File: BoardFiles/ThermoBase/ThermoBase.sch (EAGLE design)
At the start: 22 parts, among them CON1 BARREL_JACK_3PIN, U1 MOSFET_N, U2 MOSFET_N, U3 MOSFET_N, U4 LM317

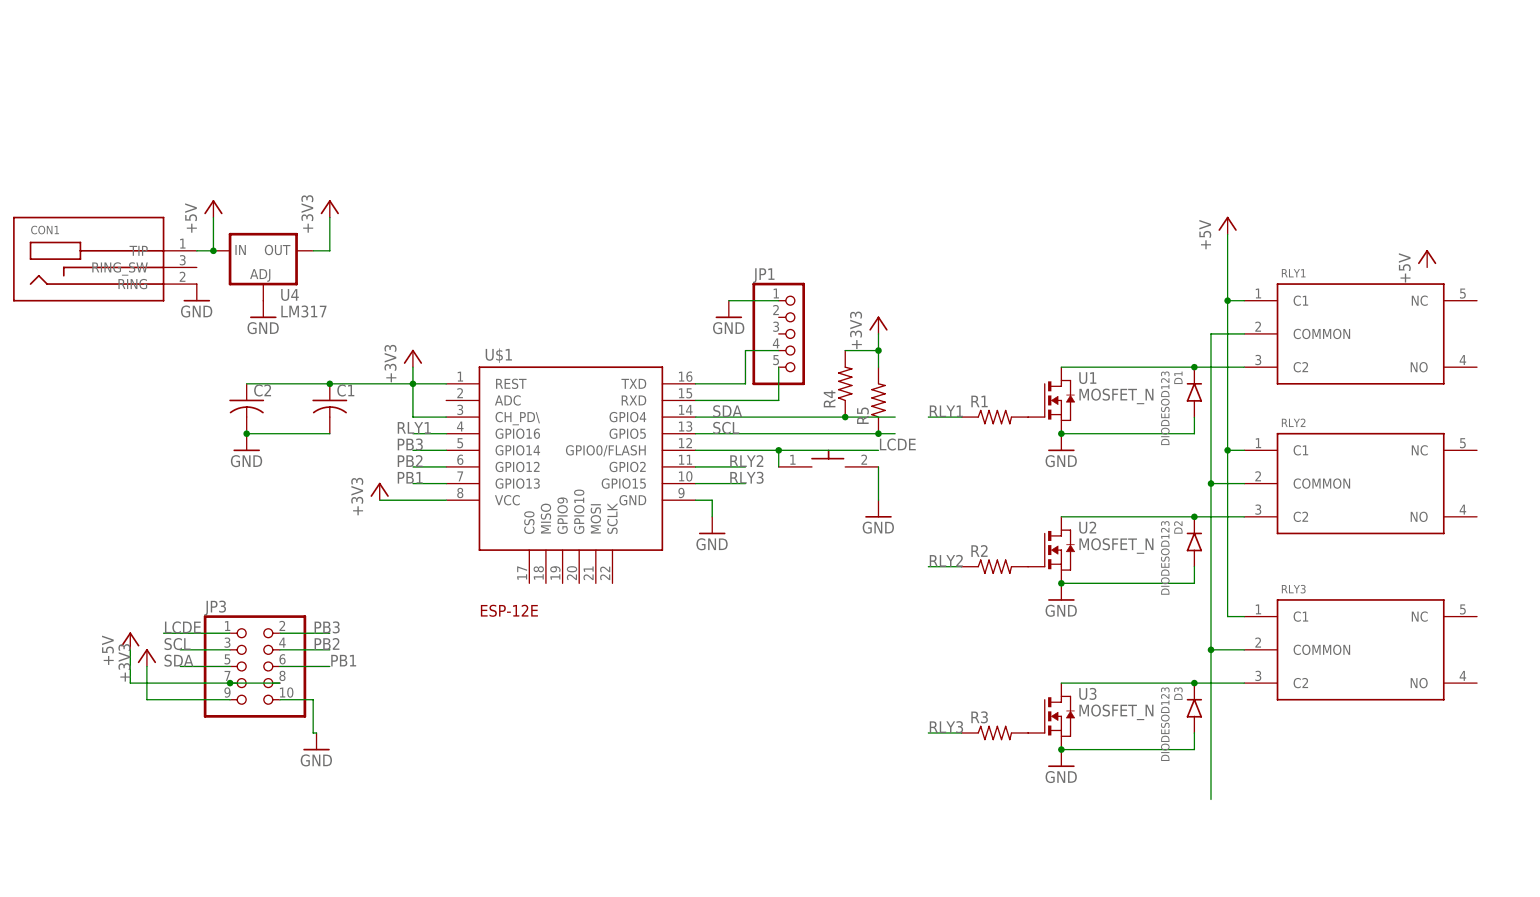
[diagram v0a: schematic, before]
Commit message: Created LCD Screen holder and updated base board to fit enclosure
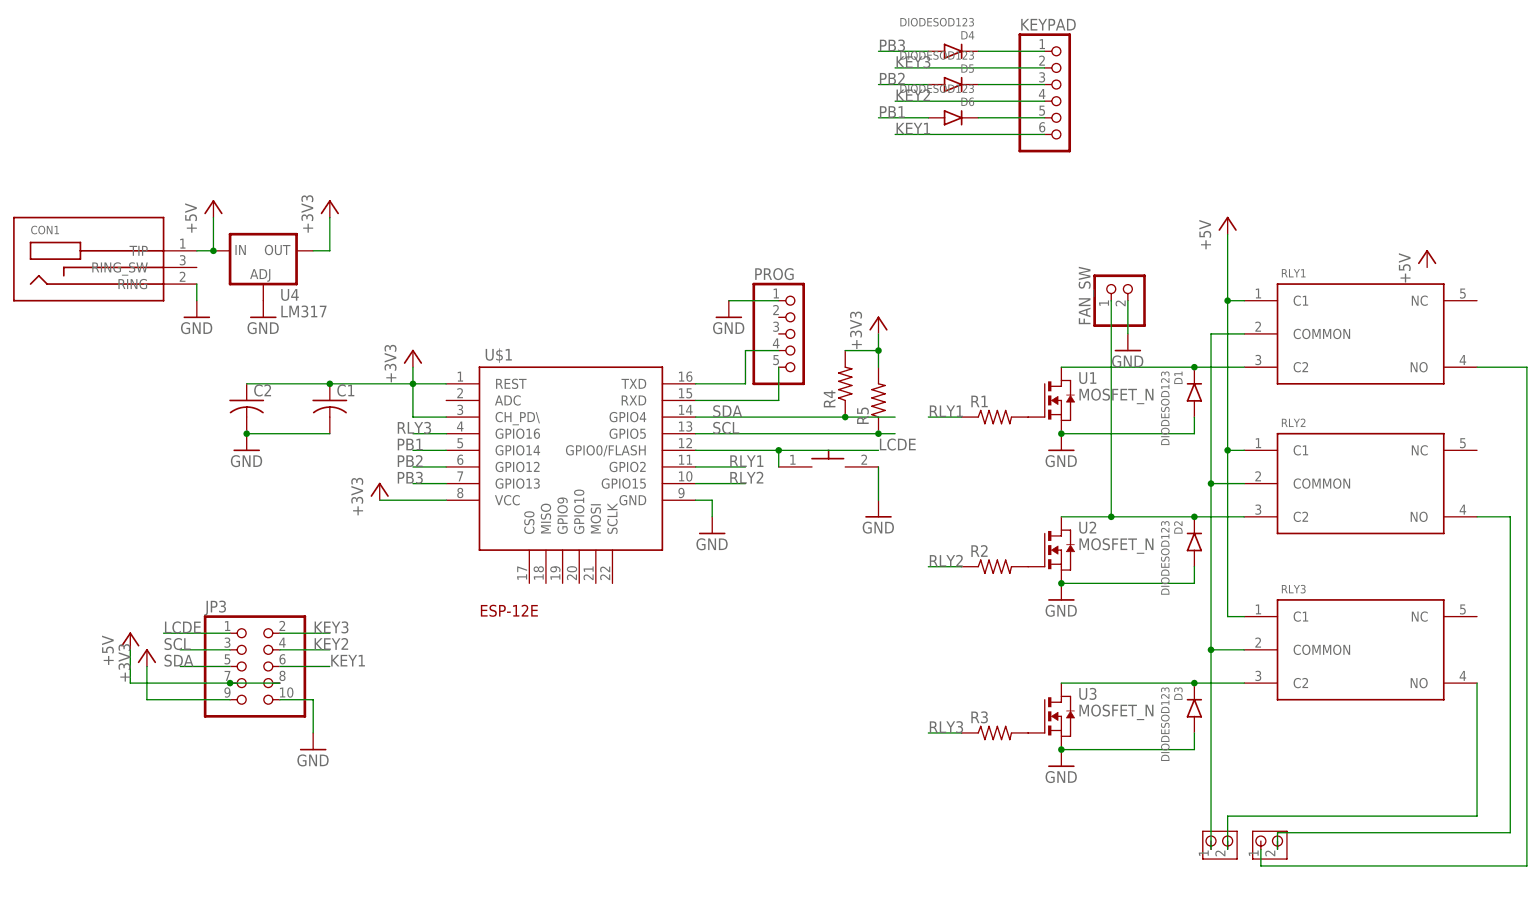
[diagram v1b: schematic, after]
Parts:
- added D4, D5, D6: DIODESOD123, DR:DIODESOD123
- added FAN_SW: (no value), pinhead:PINHD-1X2
- added H1, H2: TERMBLOCK_5MM_2POS, DR:TERMBLOCK_5MM_2POS
- added KEYPAD: (no value), pinhead:PINHD-1X6
- renumbered JP1 to PROG
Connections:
- new net KEY1: JP3.6, KEYPAD.6
- new net KEY2: JP3.4, KEYPAD.4
- new net KEY3: JP3.2, KEYPAD.2
- new net N$12: H1.2, RLY3.NO
- new net N$13: D4.C, KEYPAD.1
- new net N$14: D5.C, KEYPAD.3
- new net N$15: D6.C, KEYPAD.5
- new net N$3: H2.1, RLY1.NO
- new net N$8: H2.2, RLY2.NO
- net GND: now also FAN_SW.2
- net N$11: now also H1.1
- net N$9: now also FAN_SW.1
- net PB1: now also D6.A, U$1.GPIO14; no longer JP3.6, U$1.GPIO13
- net PB2: now also D5.A; no longer JP3.4
- net PB3: now also D4.A, U$1.GPIO13; no longer JP3.2, U$1.GPIO14
- net RLY1: now also U$1.GPIO2; no longer U$1.GPIO16
- net RLY2: now also U$1.GPIO15; no longer U$1.GPIO2
- net RLY3: now also U$1.GPIO16; no longer U$1.GPIO15

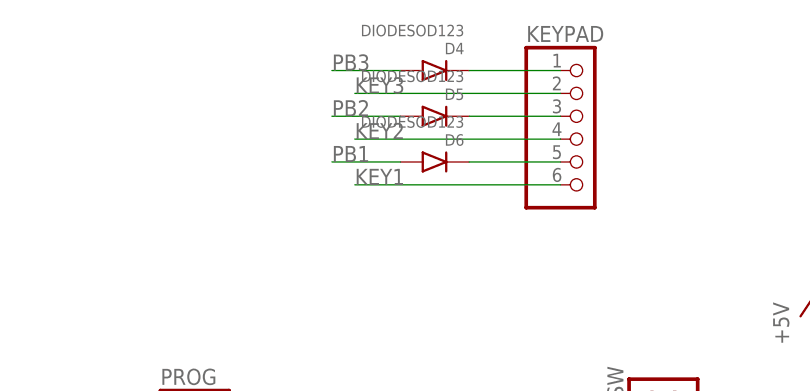
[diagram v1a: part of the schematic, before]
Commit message: Successfully built display board, archived old test software
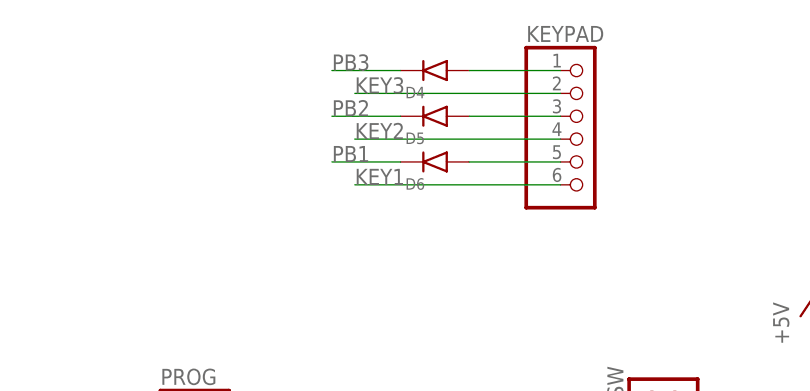
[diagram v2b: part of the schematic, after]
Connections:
- net N$13: now also D4.A; no longer D4.C
- net N$14: now also D5.A; no longer D5.C
- net N$15: now also D6.A; no longer D6.C
- net PB1: now also D6.C; no longer D6.A
- net PB2: now also D5.C; no longer D5.A
- net PB3: now also D4.C; no longer D4.A
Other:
- moved on the sheet: D4, D5, D6
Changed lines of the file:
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@@
 <part name="FAN_SW" library="pinhead" library_urn="urn:adsk.eagle:library:325" deviceset="PINHD-1X2" device="" package3d_urn="urn:adsk.eagle:package:22435/2"/>
 <part name="GND11" library="supply1" library_urn="urn:adsk.eagle:library:371" deviceset="GND" device=""/>
+<part name="KEYPAD" library="pinhead" library_urn="urn:adsk.eagle:library:325" deviceset="PINHD-1X6" device="" package3d_urn="urn:adsk.eagle:package:22472/2"/>
 <part name="D4" library="DR" deviceset="DIODE" device="SOD123"/>
-<part name="KEYPAD" library="pinhead" library_urn="urn:adsk.eagle:library:325" deviceset="PINHD-1X6" device="" package3d_urn="urn:adsk.eagle:package:22472/2"/>
 <part name="D5" library="DR" deviceset="DIODE" device="SOD123"/>
 <part name="D6" library="DR" deviceset="DIODE" device="SOD123"/>
@@
 <attribute name="VALUE" x="152.4" y="55.88" size="1.778" layer="96"/>
 </instance>
-<instance part="D4" gate="G$1" x="127" y="104.14" smashed="yes" rot="R90">
-<attribute name="NAME" x="131.556" y="107.22" size="1.27" layer="95" rot="R180"/>
-<attribute name="VALUE" x="131.556" y="109.22" size="1.27" layer="96" rot="R180"/>
-</instance>
 <instance part="KEYPAD" gate="A" x="144.78" y="96.52" smashed="yes">
 <attribute name="NAME" x="138.43" y="107.315" size="1.778" layer="95"/>
 <attribute name="VALUE" x="138.43" y="86.36" size="1.778" layer="96"/>
 </instance>
-<instance part="D5" gate="G$1" x="127" y="99.06" smashed="yes" rot="R90">
-<attribute name="NAME" x="131.556" y="102.14" size="1.27" layer="95" rot="R180"/>
-<attribute name="VALUE" x="131.556" y="104.14" size="1.27" layer="96" rot="R180"/>
-</instance>
-<instance part="D6" gate="G$1" x="127" y="93.98" smashed="yes" rot="R90">
-<attribute name="NAME" x="131.556" y="97.06" size="1.27" layer="95" rot="R180"/>
-<attribute name="VALUE" x="131.556" y="99.06" size="1.27" layer="96" rot="R180"/>
+<instance part="D4" gate="G$1" x="129.54" y="104.14" smashed="yes" rot="R270">
+<attribute name="NAME" x="124.984" y="101.06" size="1.27" layer="95"/>
+</instance>
+<instance part="D5" gate="G$1" x="129.54" y="99.06" smashed="yes" rot="R270">
+<attribute name="NAME" x="124.984" y="95.98" size="1.27" layer="95"/>
+</instance>
+<instance part="D6" gate="G$1" x="129.54" y="93.98" smashed="yes" rot="R270">
+<attribute name="NAME" x="124.984" y="90.9" size="1.27" layer="95"/>
 </instance>
 </instances>
@@
 <segment>
 <wire x1="124.46" y1="93.98" x2="116.84" y2="93.98" width="0.1524" layer="91"/>
-<pinref part="D6" gate="G$1" pin="A"/>
 <label x="116.84" y="93.98" size="1.778" layer="95"/>
+<pinref part="D6" gate="G$1" pin="C"/>
 </segment>
 <segment>
@@
 <segment>
 <wire x1="124.46" y1="99.06" x2="116.84" y2="99.06" width="0.1524" layer="91"/>
-<pinref part="D5" gate="G$1" pin="A"/>
 <label x="116.84" y="99.06" size="1.778" layer="95"/>
+<pinref part="D5" gate="G$1" pin="C"/>
 </segment>
 </net>
@@
 <segment>
 <wire x1="124.46" y1="104.14" x2="116.84" y2="104.14" width="0.1524" layer="91"/>
-<pinref part="D4" gate="G$1" pin="A"/>
 <label x="116.84" y="104.14" size="1.778" layer="95"/>
+<pinref part="D4" gate="G$1" pin="C"/>
 </segment>
 <segment>
@@
 <segment>
 <pinref part="KEYPAD" gate="A" pin="1"/>
-<pinref part="D4" gate="G$1" pin="C"/>
 <wire x1="142.24" y1="104.14" x2="132.08" y2="104.14" width="0.1524" layer="91"/>
+<pinref part="D4" gate="G$1" pin="A"/>
 </segment>
 </net>
@@
 <segment>
 <pinref part="KEYPAD" gate="A" pin="3"/>
-<pinref part="D5" gate="G$1" pin="C"/>
 <wire x1="142.24" y1="99.06" x2="132.08" y2="99.06" width="0.1524" layer="91"/>
+<pinref part="D5" gate="G$1" pin="A"/>
 </segment>
 </net>
@@
 <segment>
 <pinref part="KEYPAD" gate="A" pin="5"/>
-<pinref part="D6" gate="G$1" pin="C"/>
 <wire x1="142.24" y1="93.98" x2="132.08" y2="93.98" width="0.1524" layer="91"/>
-</segment>
-</net>
+<pinref part="D6" gate="G$1" pin="A"/>
+</segment>
+</net>

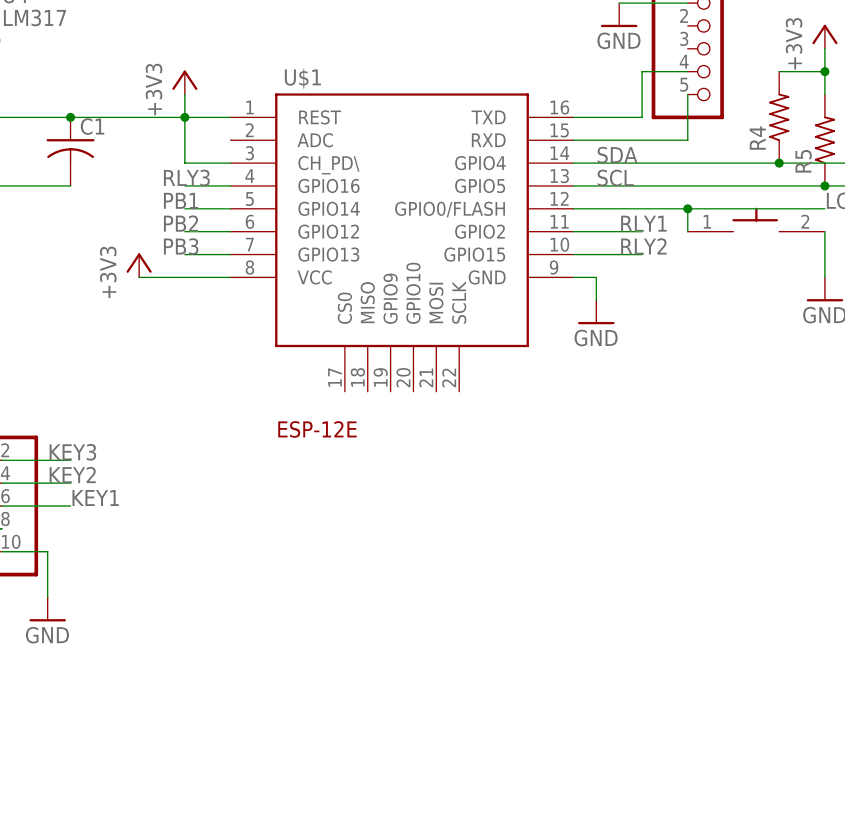
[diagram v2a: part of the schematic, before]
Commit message: Changes for keypad
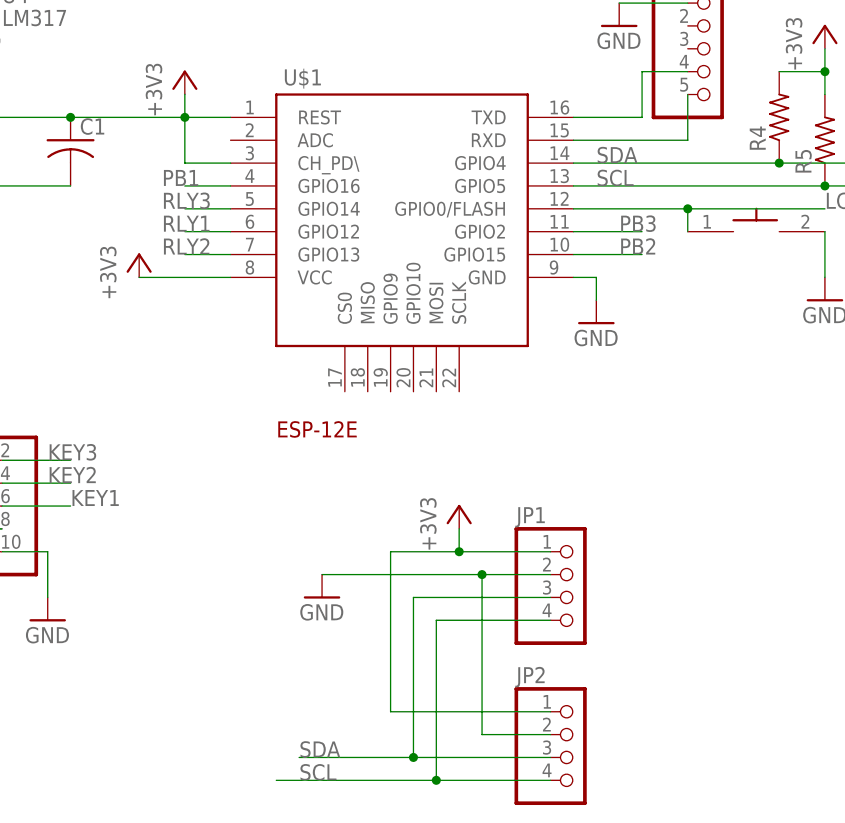
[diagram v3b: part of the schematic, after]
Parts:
- added JP1, JP2: (no value), pinhead:PINHD-1X4
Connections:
- net +3V3: now also JP1.1, JP2.1
- net GND: now also JP1.2, JP2.2
- net PB1: now also U$1.GPIO16; no longer U$1.GPIO14
- net PB2: now also U$1.GPIO15; no longer U$1.GPIO12
- net PB3: now also U$1.GPIO2; no longer U$1.GPIO13
- net RLY1: now also U$1.GPIO12; no longer U$1.GPIO2
- net RLY2: now also U$1.GPIO13; no longer U$1.GPIO15
- net RLY3: now also U$1.GPIO14; no longer U$1.GPIO16
- net SCL: now also JP1.4, JP2.4
- net SDA: now also JP1.3, JP2.3
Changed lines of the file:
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@@
 <part name="D5" library="DR" deviceset="DIODE" device="SOD123"/>
 <part name="D6" library="DR" deviceset="DIODE" device="SOD123"/>
+<part name="JP1" library="pinhead" library_urn="urn:adsk.eagle:library:325" deviceset="PINHD-1X4" device="" package3d_urn="urn:adsk.eagle:package:22407/2"/>
+<part name="JP2" library="pinhead" library_urn="urn:adsk.eagle:library:325" deviceset="PINHD-1X4" device="" package3d_urn="urn:adsk.eagle:package:22407/2"/>
+<part name="+3V6" library="supply1" library_urn="urn:adsk.eagle:library:371" deviceset="+3V3" device=""/>
+<part name="GND12" library="supply1" library_urn="urn:adsk.eagle:library:371" deviceset="GND" device=""/>
 </parts>
 <sheets>
@@
 <attribute name="NAME" x="124.984" y="90.9" size="1.27" layer="95"/>
 </instance>
+<instance part="JP1" gate="A" x="88.9" y="0" smashed="yes">
+<attribute name="NAME" x="82.55" y="8.255" size="1.778" layer="95"/>
+<attribute name="VALUE" x="82.55" y="-7.62" size="1.778" layer="96"/>
+</instance>
+<instance part="JP2" gate="A" x="88.9" y="-17.78" smashed="yes">
+<attribute name="NAME" x="82.55" y="-9.525" size="1.778" layer="95"/>
+<attribute name="VALUE" x="82.55" y="-25.4" size="1.778" layer="96"/>
+</instance>
+<instance part="+3V6" gate="G$1" x="76.2" y="10.16" smashed="yes">
+<attribute name="VALUE" x="73.66" y="5.08" size="1.778" layer="96" rot="R90"/>
+</instance>
+<instance part="GND12" gate="1" x="60.96" y="0" smashed="yes">
+<attribute name="VALUE" x="58.42" y="-2.54" size="1.778" layer="96"/>
+</instance>
 </instances>
 <busses>
@@
 <pinref part="FAN_SW" gate="G$1" pin="2"/>
 <wire x1="154.94" y1="60.96" x2="154.94" y2="66.04" width="0.1524" layer="91"/>
+</segment>
+<segment>
+<pinref part="GND12" gate="1" pin="GND"/>
+<pinref part="JP1" gate="A" pin="2"/>
+<wire x1="60.96" y1="2.54" x2="78.74" y2="2.54" width="0.1524" layer="91"/>
+<pinref part="JP2" gate="A" pin="2"/>
+<wire x1="78.74" y1="2.54" x2="86.36" y2="2.54" width="0.1524" layer="91"/>
+<wire x1="86.36" y1="-15.24" x2="78.74" y2="-15.24" width="0.1524" layer="91"/>
+<wire x1="78.74" y1="-15.24" x2="78.74" y2="2.54" width="0.1524" layer="91"/>
+<junction x="78.74" y="2.54"/>
 </segment>
 </net>
@@
 <junction x="116.84" y="58.42"/>
 </segment>
+<segment>
+<pinref part="JP1" gate="A" pin="1"/>
+<pinref part="+3V6" gate="G$1" pin="+3V3"/>
+<wire x1="86.36" y1="5.08" x2="76.2" y2="5.08" width="0.1524" layer="91"/>
+<wire x1="76.2" y1="5.08" x2="76.2" y2="7.62" width="0.1524" layer="91"/>
+<wire x1="76.2" y1="5.08" x2="68.58" y2="5.08" width="0.1524" layer="91"/>
+<junction x="76.2" y="5.08"/>
+<wire x1="68.58" y1="5.08" x2="68.58" y2="-12.7" width="0.1524" layer="91"/>
+<pinref part="JP2" gate="A" pin="1"/>
+<wire x1="68.58" y1="-12.7" x2="86.36" y2="-12.7" width="0.1524" layer="91"/>
+</segment>
 </net>
 <net name="SDA" class="0">
@@
 <label x="7.62" y="10.16" size="1.778" layer="95"/>
 </segment>
+<segment>
+<wire x1="58.42" y1="-17.78" x2="71.12" y2="-17.78" width="0.1524" layer="91"/>
+<pinref part="JP1" gate="A" pin="3"/>
+<wire x1="71.12" y1="-17.78" x2="86.36" y2="-17.78" width="0.1524" layer="91"/>
+<wire x1="86.36" y1="0" x2="71.12" y2="0" width="0.1524" layer="91"/>
+<wire x1="71.12" y1="0" x2="71.12" y2="-17.78" width="0.1524" layer="91"/>
+<junction x="71.12" y="-17.78"/>
+<pinref part="JP2" gate="A" pin="3"/>
+<label x="58.42" y="-17.78" size="1.778" layer="95"/>
+</segment>
 </net>
 <net name="SCL" class="0">
@@
 <label x="7.62" y="12.7" size="1.778" layer="95"/>
 </segment>
+<segment>
+<wire x1="55.88" y1="-20.32" x2="73.66" y2="-20.32" width="0.1524" layer="91"/>
+<pinref part="JP1" gate="A" pin="4"/>
+<wire x1="73.66" y1="-20.32" x2="86.36" y2="-20.32" width="0.1524" layer="91"/>
+<wire x1="86.36" y1="-2.54" x2="73.66" y2="-2.54" width="0.1524" layer="91"/>
+<wire x1="73.66" y1="-2.54" x2="73.66" y2="-20.32" width="0.1524" layer="91"/>
+<junction x="73.66" y="-20.32"/>
+<pinref part="JP2" gate="A" pin="4"/>
+<label x="58.42" y="-20.32" size="1.778" layer="95"/>
+</segment>
 </net>
 <net name="RLY1" class="0">
@@
 </segment>
 <segment>
-<pinref part="U$1" gate="G$1" pin="GPIO2"/>
-<wire x1="88.9" y1="40.64" x2="96.52" y2="40.64" width="0.1524" layer="91"/>
-<label x="93.98" y="40.64" size="1.778" layer="95"/>
+<pinref part="U$1" gate="G$1" pin="GPIO12"/>
+<wire x1="50.8" y1="40.64" x2="45.72" y2="40.64" width="0.1524" layer="91"/>
+<label x="43.18" y="40.64" size="1.778" layer="95"/>
 </segment>
 </net>
@@
 </segment>
 <segment>
-<pinref part="U$1" gate="G$1" pin="GPIO15"/>
-<wire x1="88.9" y1="38.1" x2="96.52" y2="38.1" width="0.1524" layer="91"/>
-<label x="93.98" y="38.1" size="1.778" layer="95"/>
+<pinref part="U$1" gate="G$1" pin="GPIO13"/>
+<wire x1="50.8" y1="38.1" x2="45.72" y2="38.1" width="0.1524" layer="91"/>
+<label x="43.18" y="38.1" size="1.778" layer="95"/>
 </segment>
 </net>
@@
 </segment>
 <segment>
-<pinref part="U$1" gate="G$1" pin="GPIO16"/>
-<wire x1="50.8" y1="45.72" x2="45.72" y2="45.72" width="0.1524" layer="91"/>
-<label x="43.18" y="45.72" size="1.778" layer="95"/>
+<pinref part="U$1" gate="G$1" pin="GPIO14"/>
+<wire x1="50.8" y1="43.18" x2="45.72" y2="43.18" width="0.1524" layer="91"/>
+<label x="43.18" y="43.18" size="1.778" layer="95"/>
 </segment>
 </net>
@@
 </segment>
 <segment>
-<pinref part="U$1" gate="G$1" pin="GPIO14"/>
-<wire x1="50.8" y1="43.18" x2="45.72" y2="43.18" width="0.1524" layer="91"/>
-<label x="43.18" y="43.18" size="1.778" layer="95"/>
+<pinref part="U$1" gate="G$1" pin="GPIO16"/>
+<wire x1="50.8" y1="45.72" x2="45.72" y2="45.72" width="0.1524" layer="91"/>
+<label x="43.18" y="45.72" size="1.778" layer="95"/>
 </segment>
 </net>
 <net name="PB2" class="0">
-<segment>
-<pinref part="U$1" gate="G$1" pin="GPIO12"/>
-<wire x1="50.8" y1="40.64" x2="45.72" y2="40.64" width="0.1524" layer="91"/>
-<label x="43.18" y="40.64" size="1.778" layer="95"/>
-</segment>
 <segment>
 <wire x1="124.46" y1="99.06" x2="116.84" y2="99.06" width="0.1524" layer="91"/>
@@
 <pinref part="D5" gate="G$1" pin="C"/>
 </segment>
+<segment>
+<pinref part="U$1" gate="G$1" pin="GPIO15"/>
+<wire x1="88.9" y1="38.1" x2="96.52" y2="38.1" width="0.1524" layer="91"/>
+<label x="93.98" y="38.1" size="1.778" layer="95"/>
+</segment>
 </net>
 <net name="PB3" class="0">
@@
 </segment>
 <segment>
-<pinref part="U$1" gate="G$1" pin="GPIO13"/>
-<wire x1="50.8" y1="38.1" x2="45.72" y2="38.1" width="0.1524" layer="91"/>
-<label x="43.18" y="38.1" size="1.778" layer="95"/>
-</segment>
-</net>
+<pinref part="U$1" gate="G$1" pin="GPIO2"/>
+<wire x1="88.9" y1="40.64" x2="96.52" y2="40.64" width="0.1524" layer="91"/>
+<label x="93.98" y="40.64" size="1.778" layer="95"/>
+</segment>
+</net>
